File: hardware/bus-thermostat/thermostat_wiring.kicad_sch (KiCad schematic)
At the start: 35 parts, among them Q1 IRF540N, Q2 IRF540N, Q3 2N7002, Q4 2N7002, Q5 2N7002, T1 1:2/0.5, U1 NE555PWR, U2 TLV9301IDCK, U3 LTC7060EMSE

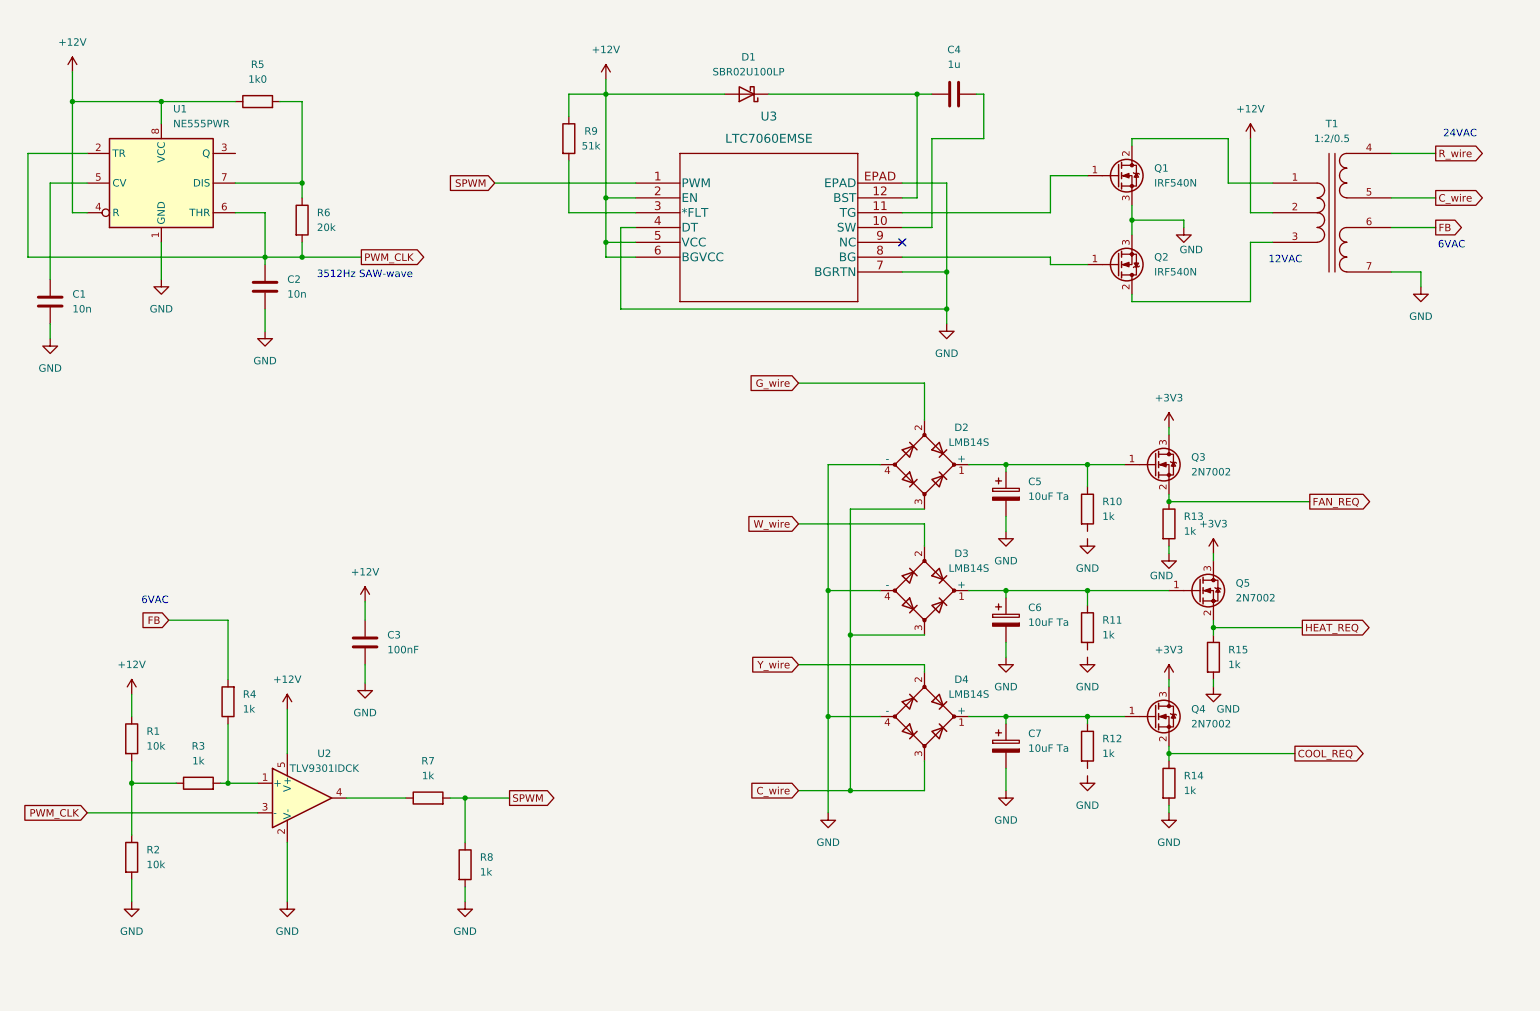
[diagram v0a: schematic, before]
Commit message: Changing the SPWM around
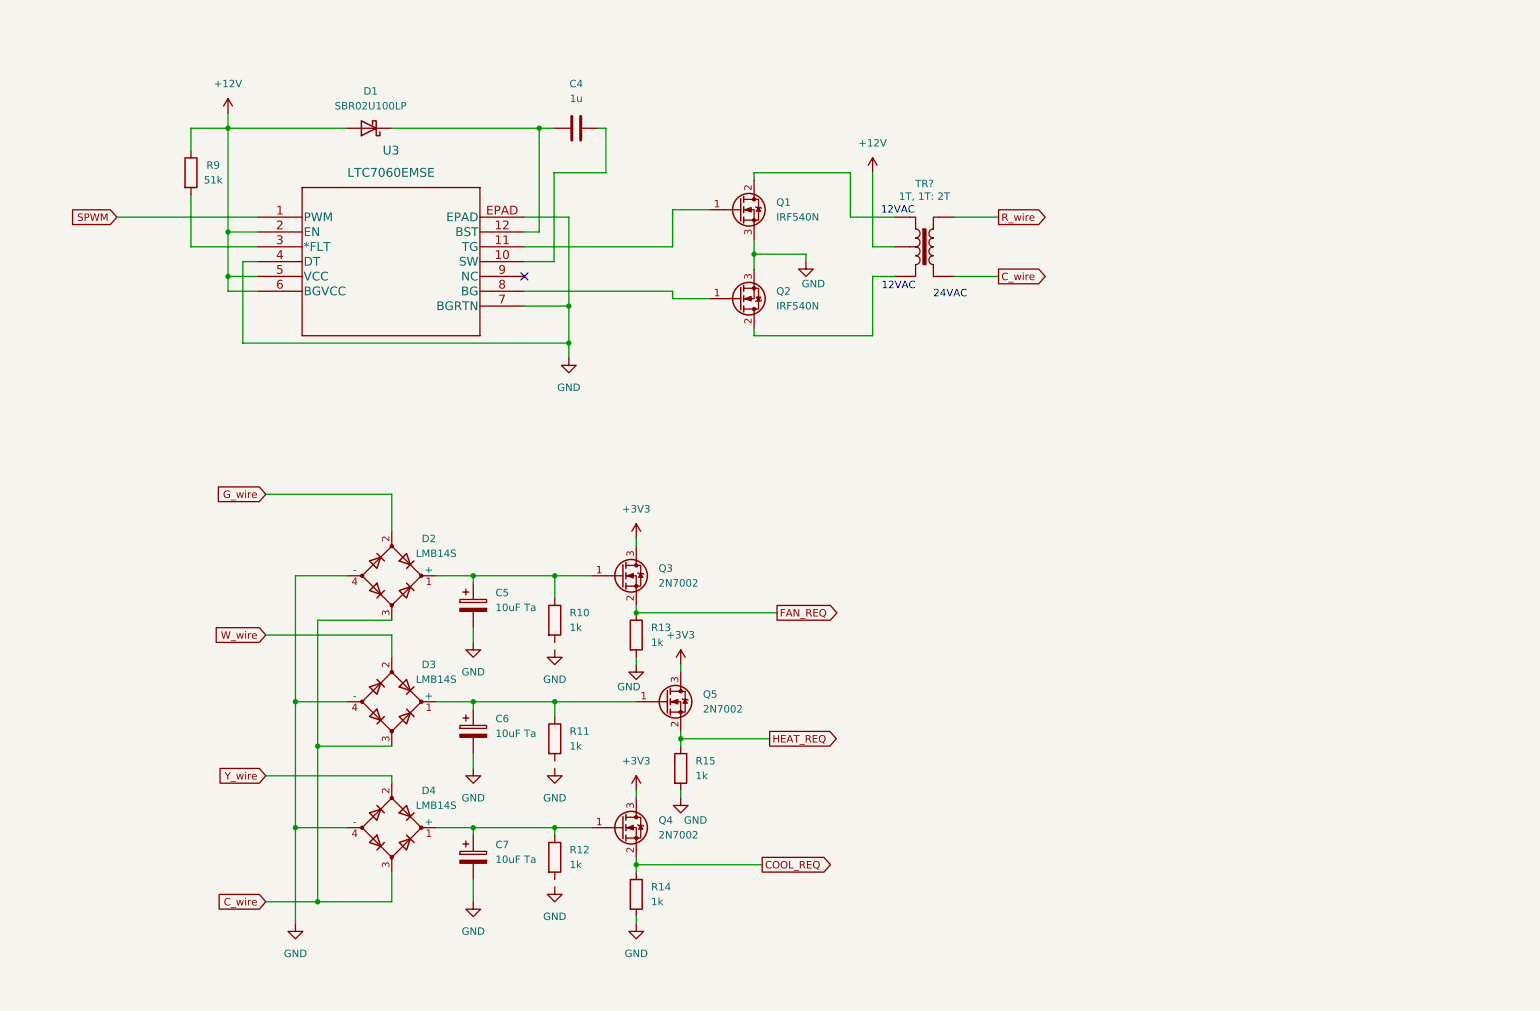
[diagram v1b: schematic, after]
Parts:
- removed C1, C2: 10n, symbol Device:C
- removed C3: 100nF, symbol Device:C
- removed R1, R2: 10k, symbol Device:R
- removed R3, R4, R7, R8: 1k, symbol Device:R
- removed R5: 1k0, symbol Device:R
- removed R6: 20k, symbol Device:R
- removed T1: 1:2/0.5, symbol Device:Transformer_SP_2S
- removed U1: NE555PWR, Package_SO:TSSOP-8_4.4x3mm_P0.65mm, symbol Timer:NE555P
- removed U2: TLV9301IDCK, Package_TO_SOT_SMD:SOT-353_SC-70-5, symbol Amplifier_Operational:TLV9001IDCK
- added TR?: 1T, 1T: 2T, symbol Transformer:TRANSF4
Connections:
- net +12V: now also TR?.2
- net C_wire: now also TR?.4
- net R_wire: now also TR?.5
- net at Q1.2 (D): now also TR?.1
- net at Q2.2 (D): now also TR?.3
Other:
- note removed: "3512Hz SAW-wave"
- note removed: "6VAC"
- moved on the sheet: C4, C5, C6, C7, D1, D2, D3, D4, Q1, Q2, Q3, Q4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

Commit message: Redid the 24VAC path entirely.
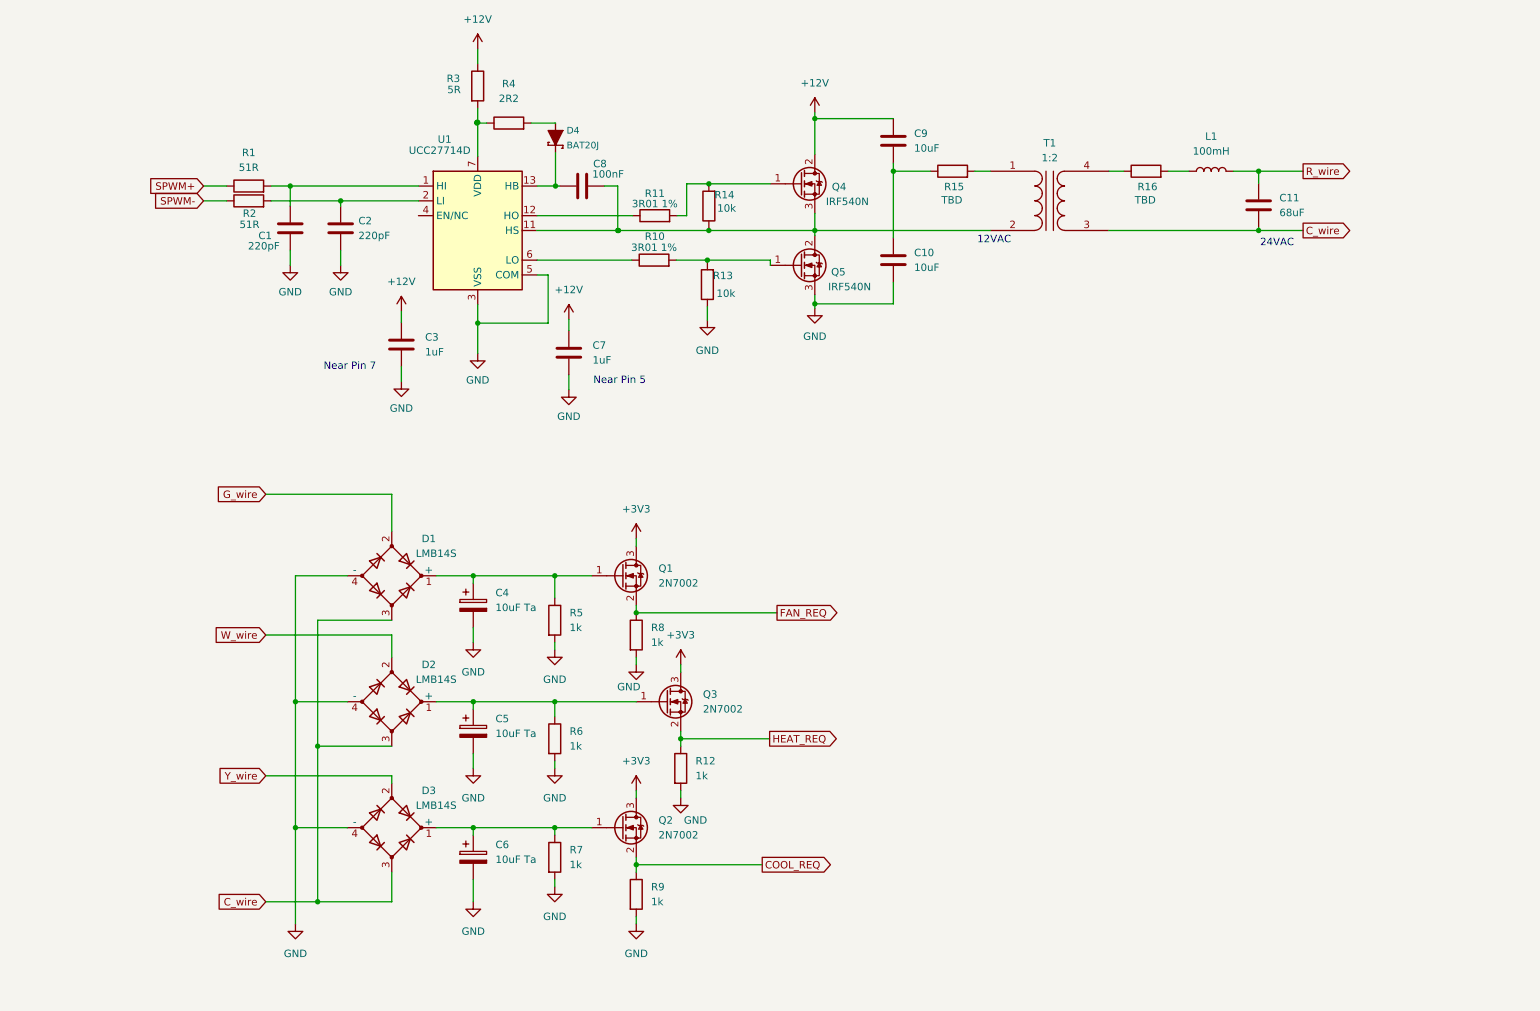
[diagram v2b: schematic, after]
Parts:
- removed C4: 1u, symbol Device:C
- removed D1: SBR02U100LP, Diode_SMD:D_0402_1005Metric_Pad0.77x0.64mm_HandSolder, symbol Device:D_Schottky
- removed R9: 51k, symbol Device:R
- removed TR?: 1T, 1T: 2T, symbol Transformer:TRANSF4
- removed U3: LTC7060EMSE, Package_SO:MSOP-12-1EP_3x4mm_P0.65mm_EP1.65x2.85mm_ThermalVias, symbol UltraLibrarian:LTC7060JMSE-WTRPBF
- added C1, C2: 220pF, symbol Device:C
- added C10, C9: 10uF, symbol Device:C
- added C11: 68uF, symbol Device:C
- added C3, C7: 1uF, symbol Device:C
- added C8: 100nF, symbol Device:C
- added D4: BAT20J, SparkFun-Silicon-Standard:SOD-323, symbol SparkFun-DiscreteSemi:DIODE-SCHOTTKY-BAT20J
- added L1: 100mH, symbol Device:L
- added R1, R2: 51R, symbol Device:R
- added R10, R11: 3R01 1%, symbol Device:R
- added R13, R14: 10k, symbol Device:R
- added R15, R16: TBD, symbol Device:R
- added R3: 5R, symbol Device:R
- added R4: 2R2, symbol Device:R
- added T1: 1:2, Transformer_THT:Transformer_Toroid_Horizontal_D9.0mm_Amidon-T30, symbol Device:Transformer_1P_1S
- added U1: UCC27714D, Package_SO:SOIC-14_3.9x8.7mm_P1.27mm, symbol Driver_FET:UCC27714D
- D1: renamed from D2; footprint Diode_SMD:Diode_Bridge_OnSemi_SDIP-4L -> Diode_SMD:Diode_Bridge_Vishay_MBLS
- D2: renamed from D3; footprint Diode_SMD:Diode_Bridge_OnSemi_SDIP-4L -> Diode_SMD:Diode_Bridge_Vishay_MBLS
- D3: renamed from D4; footprint Diode_SMD:Diode_Bridge_OnSemi_SDIP-4L -> Diode_SMD:Diode_Bridge_Vishay_MBLS
- renumbered C5 to C4, C6 to C5, C7 to C6, Q3 to Q1, Q4 to Q2, Q5 to Q3, Q1 to Q4, Q2 to Q5, R15 to R12, R10 to R5, R11 to R6, R12 to R7, R13 to R8, R14 to R9
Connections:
- net +12V: now also Q4.2 (D), C3.1, C7.1, C9.1, R3.1
- net C_wire: now also C11.2, T1.3 (SA)
- net GND: now also R5.2, R6.2, R7.2, C1.2, C10.2, C2.2, C3.2, C7.2, R13.1, U1.3 (VSS), U1.5 (COM); no longer Q4.3 (S)
- net R_wire: now also C11.1, L1.2
- net at Q5.2 (D): now also Q4.3 (S), R14.1, T1.2 (AB)
- net at Q4.1 (G): now also R11.2, R14.2
- net at Q5.1 (G): now also R10.2, R13.2
- new net: C10.1, C9.2, R15.1
- new net: C2.1, R2.2, U1.2 (LI)
- new net: R3.2, R4.1, U1.7 (VDD)
- new net: D4.A, R4.2
- new net: C8.1, D4.C, U1.13 (HB)
- new net: C1.1, R1.2, U1.1 (HI)
- new net: R15.2, T1.1 (AA)
- new net: R16.1, T1.4 (SB)
- new net: R10.1, U1.6 (LO)
- new net: R11.1, U1.12 (HO)
- new net: L1.1, R16.2
- new net: C8.2, U1.11 (HS)
- new net SPWM+: R1.1
- new net SPWM-: R2.1
- no-connect marks 1 -> 0
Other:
- note added: "Near Pin 5"
- note added: "Near Pin 7"
- moved on the sheet: Q4, Q5

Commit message: First rev of thermostat firmware
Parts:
- added R? (x2): 10k, symbol Device:R
- added U?: PCA9557D, Package_SO:SOP-16_3.9x9.9mm_P1.27mm, symbol Interface_Expansion:PCA9557D
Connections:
- net +3V3: now also U?.16 (VDD)
- net COOL_REQ: now also U?.9 (IO2)
- net FAN_REQ: now also U?.6 (IO0)
- net GND: now also R?.2, R?.2, U?.3 (A0), U?.4 (A1), U?.5 (A2), U?.8 (VSS)
- net HEAT_REQ: now also U?.7 (IO1)
- net EN_24VAC: now reaches U1.4 (EN/NC)
- net EN_24VAC: now also R?.1, U?.14 (IO7)
- new net I2C_EN: R?.1, U?.13 (IO6)
- new net SCL: U?.1 (SCL)
- new net SDA: U?.2 (SDA)
- new net ~{RESET}: U?.15 (~{RESET})
- no-connect marks 0 -> 3
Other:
- note added: "I2C Address 0x18-1F We will use 0x18"

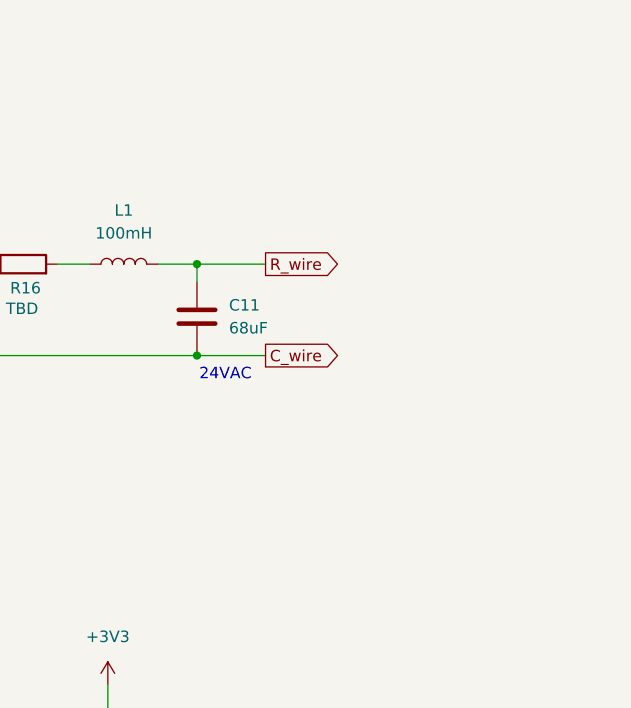
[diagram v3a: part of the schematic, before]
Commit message: OK, we will need the R wire!  Also put in option to use 12VDC
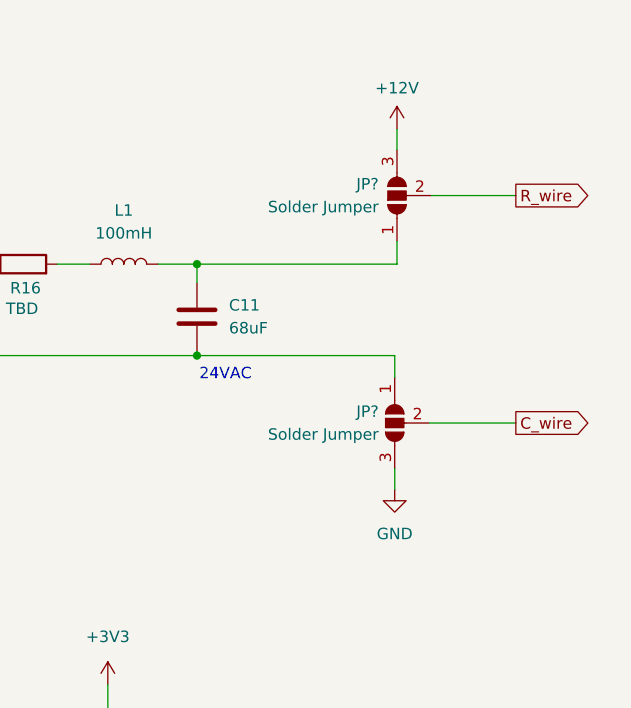
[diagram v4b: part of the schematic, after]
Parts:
- added JP? (x2): Solder Jumper, Jumper:SolderJumper-3_P2.0mm_Open_TrianglePad1.0x1.5mm, symbol Jumper:SolderJumper_3_Open
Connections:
- net +12V: now also JP?.3 (B)
- net C_wire: now also JP?.2 (C); no longer C11.2, T1.3 (SA)
- net GND: now also JP?.3 (B)
- net R_wire: now also JP?.2 (C); no longer C11.1, L1.2
- new net: C11.2, JP?.1 (A), T1.3 (SA)
- new net: C11.1, JP?.1 (A), L1.2
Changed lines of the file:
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@@
+    (stroke (width 0) (type default) (color 0 0 0 0))
+  )
+  (wire (pts (xy 262.128 66.421) (xy 262.128 68.707))
     (stroke (width 0) (type default) (color 0 0 0 0))
   )
@@
     (stroke (width 0) (type default) (color 0 0 0 0))
   )
-  (wire (pts (xy 240.157 43.688) (xy 247.777 43.688))
+  (wire (pts (xy 240.157 43.688) (xy 262.382 43.688))
     (stroke (width 0) (type default) (color 0 0 0 0))
   )
@@
     (stroke (width 0) (type default) (color 0 0 0 0))
   )
+  (wire (pts (xy 262.128 53.848) (xy 262.128 56.261))
+    (stroke (width 0) (type default) (color 0 0 0 0))
+  )
   (wire (pts (xy 107.823 35.433) (xy 106.172 35.433))
     (stroke (width 0) (type default) (color 0 0 0 0))
@@
     (stroke (width 0) (type default) (color 0 0 0 0))
   )
+  (wire (pts (xy 265.938 61.341) (xy 275.59 61.341))
+    (stroke (width 0) (type default) (color 0 0 0 0))
+  )
   (wire (pts (xy 164.084 53.848) (xy 164.084 54.737))
     (stroke (width 0) (type default) (color 0 0 0 0))
@@
     (stroke (width 0) (type default) (color 0 0 0 0))
   )
+  (wire (pts (xy 266.192 36.068) (xy 275.59 36.068))
+    (stroke (width 0) (type default) (color 0 0 0 0))
+  )
   (wire (pts (xy 119.507 156.21) (xy 125.857 156.21))
     (stroke (width 0) (type default) (color 0 0 0 0))
@@
     (stroke (width 0) (type default) (color 0 0 0 0))
   )
+  (wire (pts (xy 262.382 28.702) (xy 262.382 30.988))
+    (stroke (width 0) (type default) (color 0 0 0 0))
+  )
   (wire (pts (xy 133.477 119.38) (xy 157.607 119.38))
     (stroke (width 0) (type default) (color 0 0 0 0))
   )
-  (wire (pts (xy 240.157 53.848) (xy 247.777 53.848))
+  (wire (pts (xy 240.157 53.848) (xy 262.128 53.848))
     (stroke (width 0) (type default) (color 0 0 0 0))
   )
@@
   )
   (wire (pts (xy 130.302 53.848) (xy 130.302 46.228))
+    (stroke (width 0) (type default) (color 0 0 0 0))
+  )
+  (wire (pts (xy 262.382 41.148) (xy 262.382 43.688))
     (stroke (width 0) (type default) (color 0 0 0 0))
   )
@@
     )
   )
-  (global_label "C_wire" (shape output) (at 247.777 53.848 0) (fields_autoplaced)
+  (global_label "C_wire" (shape output) (at 275.59 61.341 0) (fields_autoplaced)
     (effects (font (size 1.27 1.27)) (justify left))
-    (property "Intersheet References" "${INTERSHEET_REFS}" (id 0) (at 256.2377 53.7686 0)
+    (property "Intersheet References" "${INTERSHEET_REFS}" (id 0) (at 284.0507 61.2616 0)
       (effects (font (size 1.27 1.27)) (justify left) hide)
     )
@@
     )
   )
-  (global_label "R_wire" (shape output) (at 247.777 43.688 0) (fields_autoplaced)
+  (global_label "R_wire" (shape output) (at 275.59 36.068 0) (fields_autoplaced)
     (effects (font (size 1.27 1.27)) (justify left))
-    (property "Intersheet References" "${INTERSHEET_REFS}" (id 0) (at 256.2377 43.6086 0)
+    (property "Intersheet References" "${INTERSHEET_REFS}" (id 0) (at 284.0507 35.9886 0)
       (effects (font (size 1.27 1.27)) (justify left) hide)
     )
@@
     (pin "3")
   )
+  (symbol (lib_name "GND_6") (lib_id "power:GND") (at 262.128 68.707 0) (unit 1)
+    (in_bom yes) (on_board yes) (fields_autoplaced)
+    (property "Reference" "#PWR?" (id 0) (at 262.128 75.057 0)
+      (effects (font (size 1.27 1.27)) hide)
+    )
+    (property "Value" "GND" (id 1) (at 262.128 73.66 0))
+    (property "Footprint" "" (id 2) (at 262.128 68.707 0)
+      (effects (font (size 1.27 1.27)) hide)
+    )
+    (property "Datasheet" "" (id 3) (at 262.128 68.707 0)
+      (effects (font (size 1.27 1.27)) hide)
+    )
+    (pin "1")
+  )
   (symbol (lib_id "Device:C_Polarized") (at 105.537 161.29 0) (unit 1)
     (in_bom yes) (on_board yes) (fields_autoplaced)
@@
     (pin "1")
   )
+  (symbol (lib_id "Jumper:SolderJumper_3_Open") (at 262.128 61.341 90) (mirror x) (unit 1)
+    (in_bom yes) (on_board yes) (fields_autoplaced)
+    (property "Reference" "JP?" (id 0) (at 260.35 60.0709 90)
+      (effects (font (size 1.27 1.27)) (justify left))
+    )
+    (property "Value" "Solder Jumper" (id 1) (at 260.35 62.6109 90)
+      (effects (font (size 1.27 1.27)) (justify left))
+    )
+    (property "Footprint" "Jumper:SolderJumper-3_P2.0mm_Open_TrianglePad1.0x1.5mm" (id 2) (at 262.128 61.341 0)
+      (effects (font (size 1.27 1.27)) hide)
+    )
+    (property "Datasheet" "~" (id 3) (at 262.128 61.341 0)
+      (effects (font (size 1.27 1.27)) hide)
+    )
+    (pin "1")
+    (pin "2")
+    (pin "3")
+  )
   (symbol (lib_id "Device:R") (at 136.525 58.928 90) (unit 1)
     (in_bom yes) (on_board yes)
@@
     (pin "2")
   )
+  (symbol (lib_name "+12V_1") (lib_id "power:+12V") (at 262.382 28.702 0) (unit 1)
+    (in_bom yes) (on_board yes) (fields_autoplaced)
+    (property "Reference" "#PWR?" (id 0) (at 262.382 32.512 0)
+      (effects (font (size 1.27 1.27)) hide)
+    )
+    (property "Value" "+12V" (id 1) (at 262.382 24.13 0))
+    (property "Footprint" "" (id 2) (at 262.382 28.702 0)
+      (effects (font (size 1.27 1.27)) hide)
+    )
+    (property "Datasheet" "" (id 3) (at 262.382 28.702 0)
+      (effects (font (size 1.27 1.27)) hide)
+    )
+    (pin "1")
+  )
   (symbol (lib_id "power:GND") (at 141.097 151.13 0) (unit 1)
     (in_bom yes) (on_board yes)
@@
     (pin "2")
   )
+  (symbol (lib_id "Jumper:SolderJumper_3_Open") (at 262.382 36.068 90) (unit 1)
+    (in_bom yes) (on_board yes) (fields_autoplaced)
+    (property "Reference" "JP?" (id 0) (at 260.35 34.7979 90)
+      (effects (font (size 1.27 1.27)) (justify left))
+    )
+    (property "Value" "Solder Jumper" (id 1) (at 260.35 37.3379 90)
+      (effects (font (size 1.27 1.27)) (justify left))
+    )
+    (property "Footprint" "Jumper:SolderJumper-3_P2.0mm_Open_TrianglePad1.0x1.5mm" (id 2) (at 262.382 36.068 0)
+      (effects (font (size 1.27 1.27)) hide)
+    )
+    (property "Datasheet" "~" (id 3) (at 262.382 36.068 0)
+      (effects (font (size 1.27 1.27)) hide)
+    )
+    (pin "1")
+    (pin "2")
+    (pin "3")
+  )
   (symbol (lib_id "Driver_FET:UCC27714D") (at 106.299 53.848 0) (unit 1)

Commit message: Add some text
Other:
- note added: "Pin 1-2 - 24VAC Pin 2-3 - 12VDC"
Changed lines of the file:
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@@
+    (effects (font (size 1.27 1.27)) (justify left bottom))
+  )
+  (text "Pin 1-2 - 24VAC\nPin 2-3 - 12VDC" (at 264.287 50.673 0)
     (effects (font (size 1.27 1.27)) (justify left bottom))
   )
